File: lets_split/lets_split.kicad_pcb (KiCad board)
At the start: 2 copper layers, 114.2 x 82 mm, 79 parts, among them J1 Speaker, P1 USB-rewire, P2 USB_OTG, P3 WS2812, P4 TRRS jack, SW1 SW_PUSH, SW10 SW_PUSH, SW11 SW_PUSH, SW12 SW_PUSH, SW13 SW_PUSH, SW14 SW_PUSH, SW15 SW_PUSH, SW16 SW_PUSH, SW17 SW_PUSH, SW18 SW_PUSH, SW19 SW_PUSH, SW2 SW_PUSH, SW20 SW_PUSH, SW21 SW_PUSH, SW22 SW_PUSH, SW23 SW_PUSH, SW24 SW_PUSH, SW3 SW_PUSH, SW4 SW_PUSH, SW5 SW_PUSH, SW6 SW_PUSH, SW7 SW_PUSH, SW8 SW_PUSH, SW9 SW_PUSH, U1 ArduinoProMicro

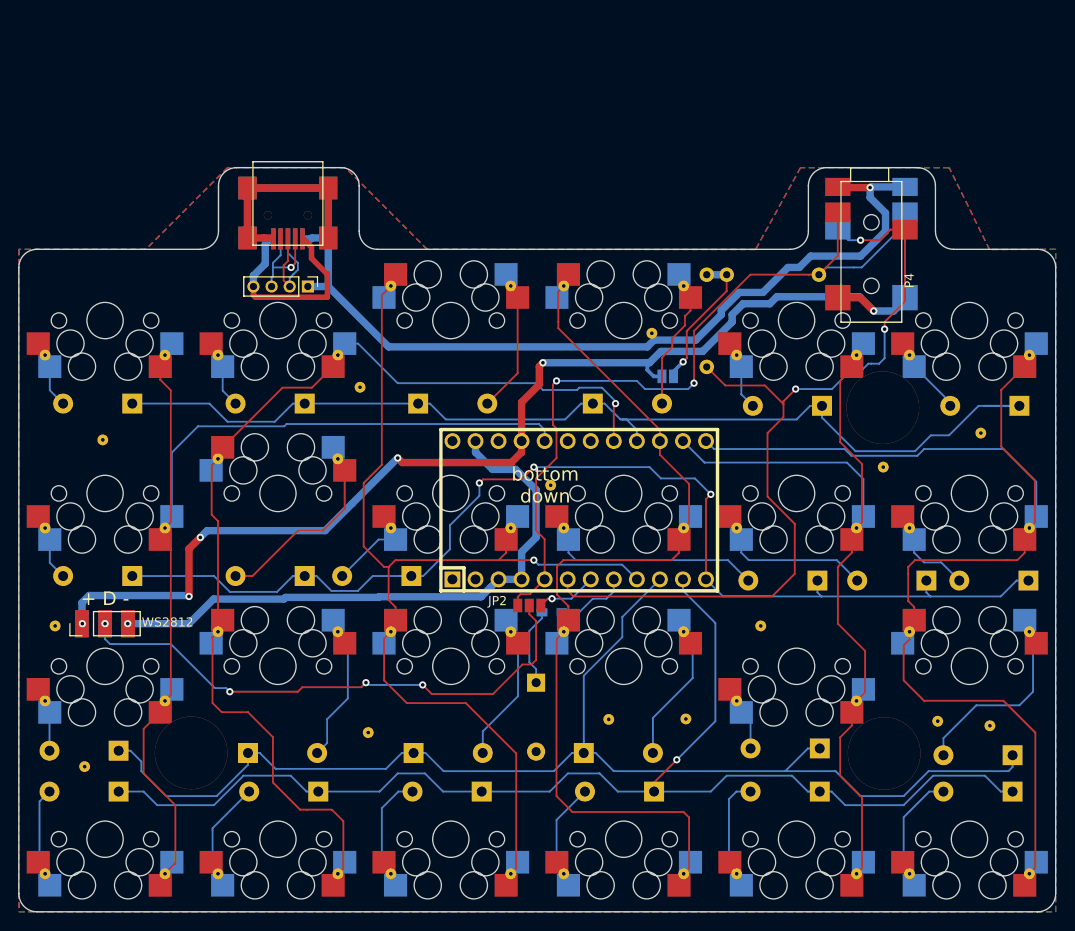
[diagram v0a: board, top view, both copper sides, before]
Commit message: Did a few small changes to routing
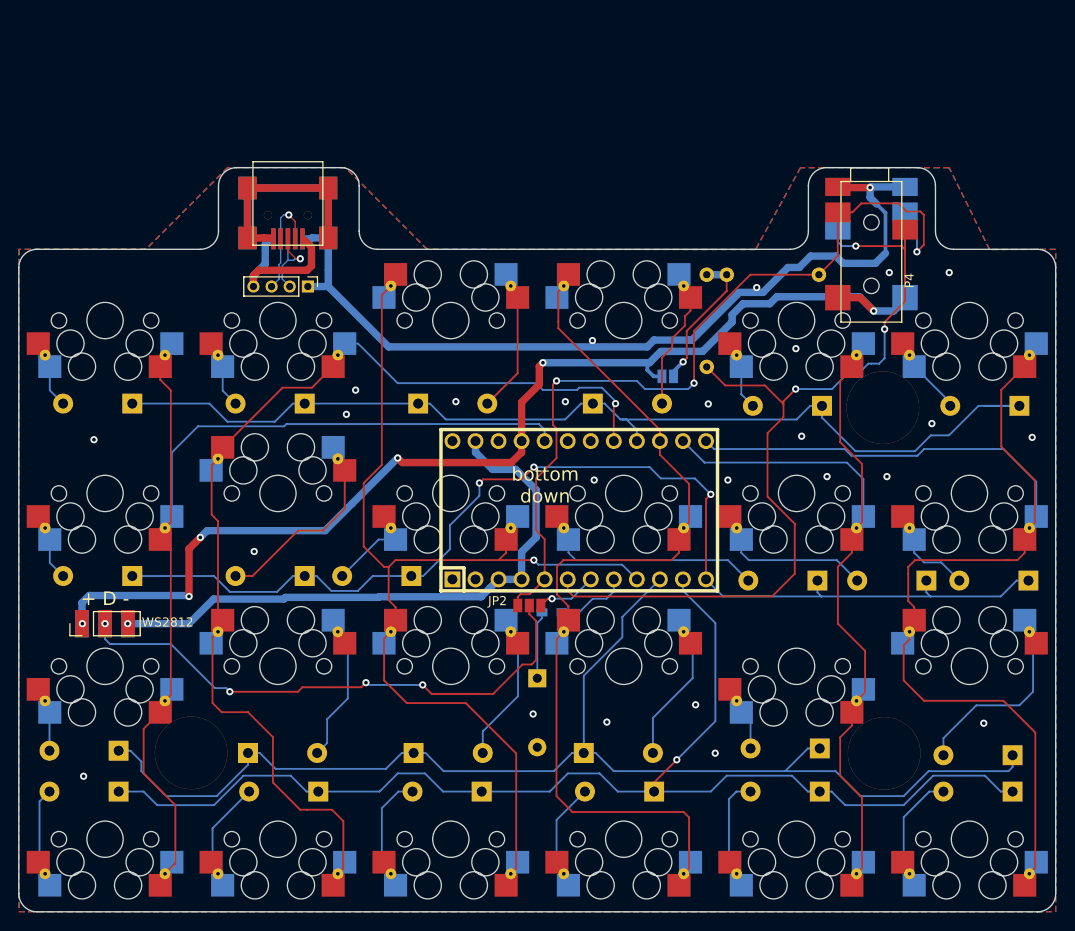
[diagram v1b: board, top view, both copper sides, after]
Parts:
- removed the REF** at (139.6, 91.0)
- removed the REF** at (176.2, 89.0)
- removed the REF** at (150.8, 74.2)
- removed the REF** at (88.2, 122.0)
- removed the REF** at (85.0, 106.5)
- removed the REF** at (90.2, 86.0)
- removed the REF** at (118.6, 80.2)
- removed the REF** at (188.0, 117.5)
- removed the REF** at (154.5, 116.8)
- removed the REF** at (182.2, 117.0)
- removed the REF** at (162.8, 106.5)
- removed the REF** at (119.5, 118.2)
- removed the REF** at (146.0, 116.8)
- removed the REF** at (187.0, 85.2)
- P3: value WS2812 -> WS2812-Strip
- moved J1 0.50 mm to (138.1, 112.3)
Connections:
- P2 pad 4: (no net) -> Net-(P2-Pad4)
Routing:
- net SDA: track 86.9 -> 93.5 mm, vias 2 -> 3
- net Net-(P1-Pad4): track 23.4 -> 18.1 mm
- net GND: track 201.0 -> 202.9 mm, vias 2 -> 27
- net /D+: track 11.8 -> 10.3 mm, vias 0 -> 1
- net Net-(J1-Pad1): track 8.64 -> 7.49 mm
- net /D-: track 11.0 -> 11.9 mm
- net SCL/D3: track 95.3 -> 96.0 mm
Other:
- net class Default: trace_width 0.25 -> 0.1524

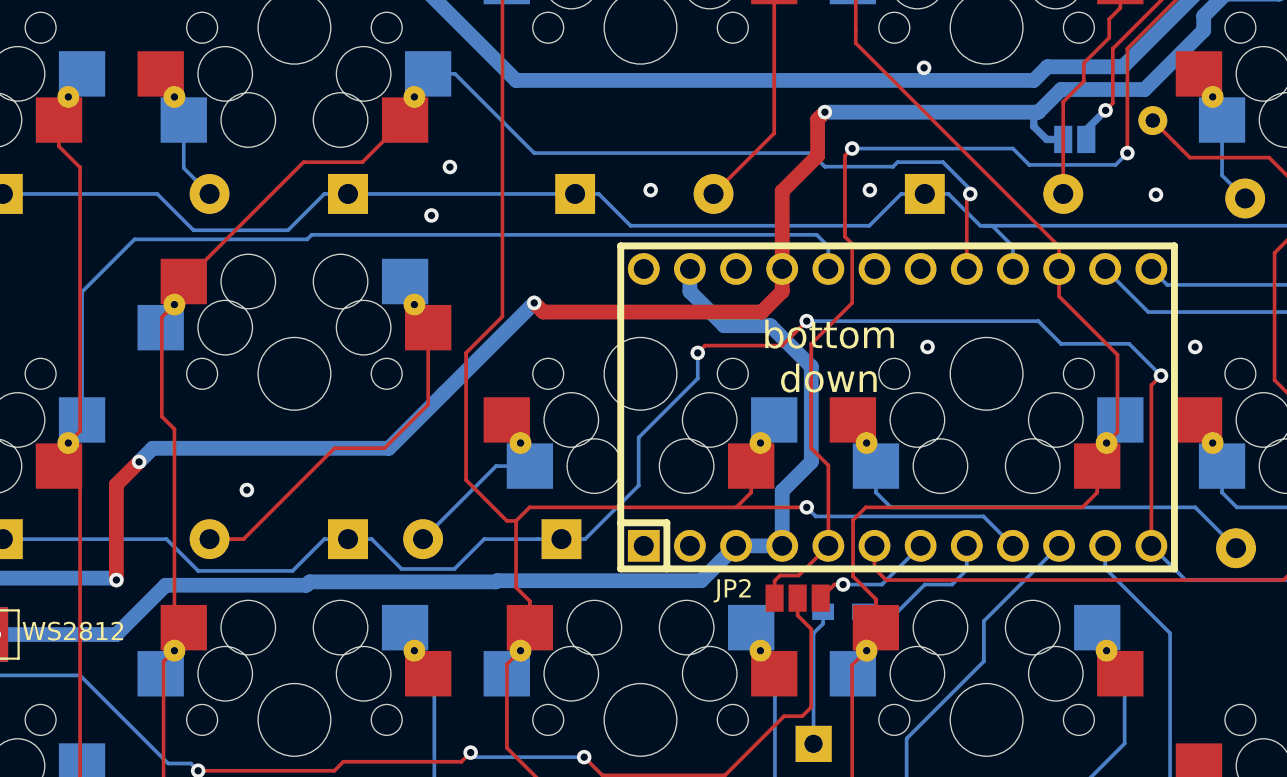
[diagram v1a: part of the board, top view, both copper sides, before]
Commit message: Fixed a broken gnd path
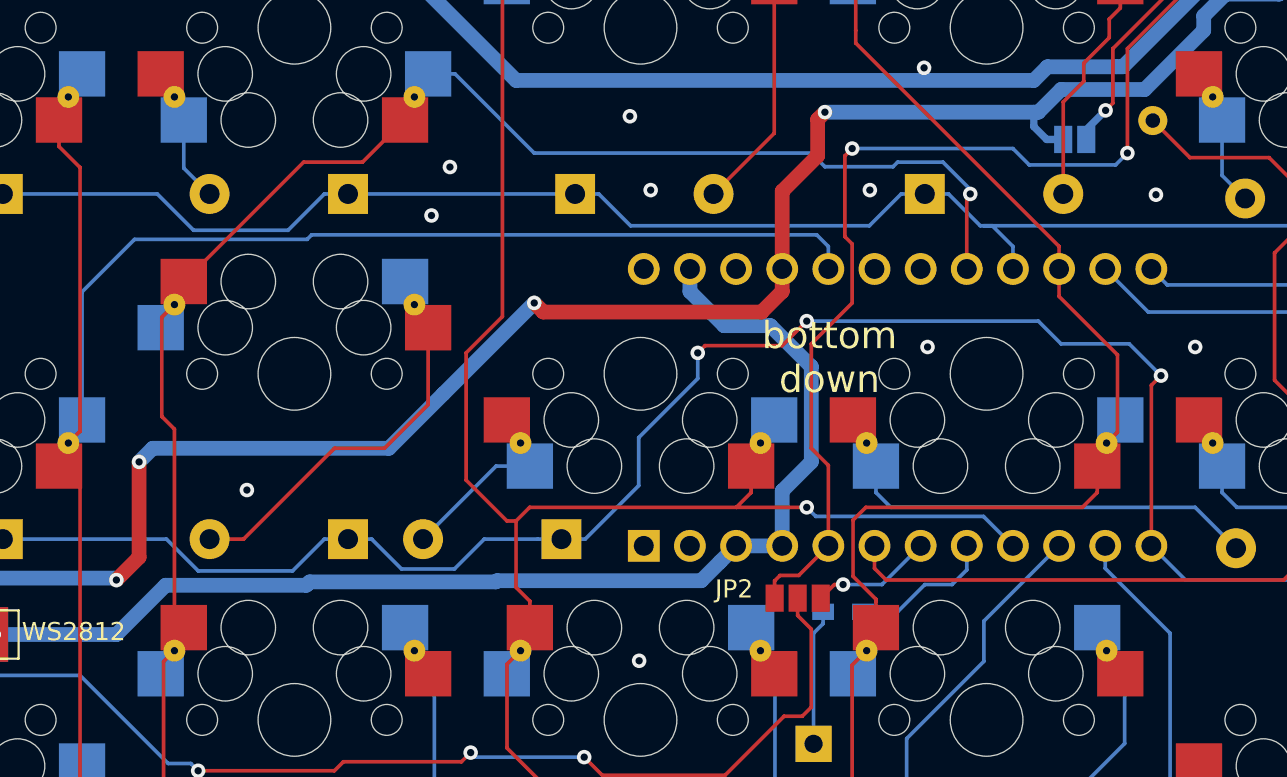
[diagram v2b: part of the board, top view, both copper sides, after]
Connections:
- P2 pad 4: Net-(P2-Pad4) -> (no net) (x2)
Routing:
- net GND: vias 27 -> 29
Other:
- net class Default: trace_width 0.1524 -> 0.25

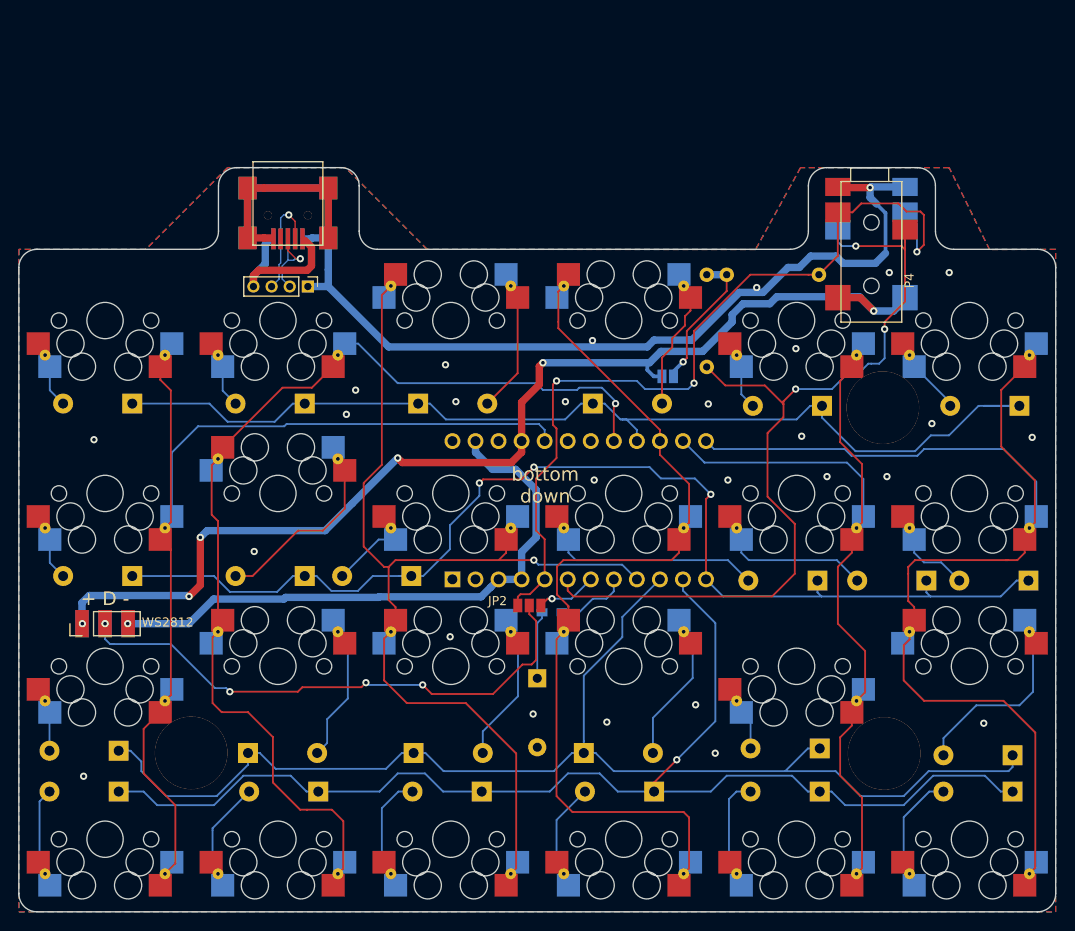
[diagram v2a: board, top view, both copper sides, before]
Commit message: Added speaker symbol
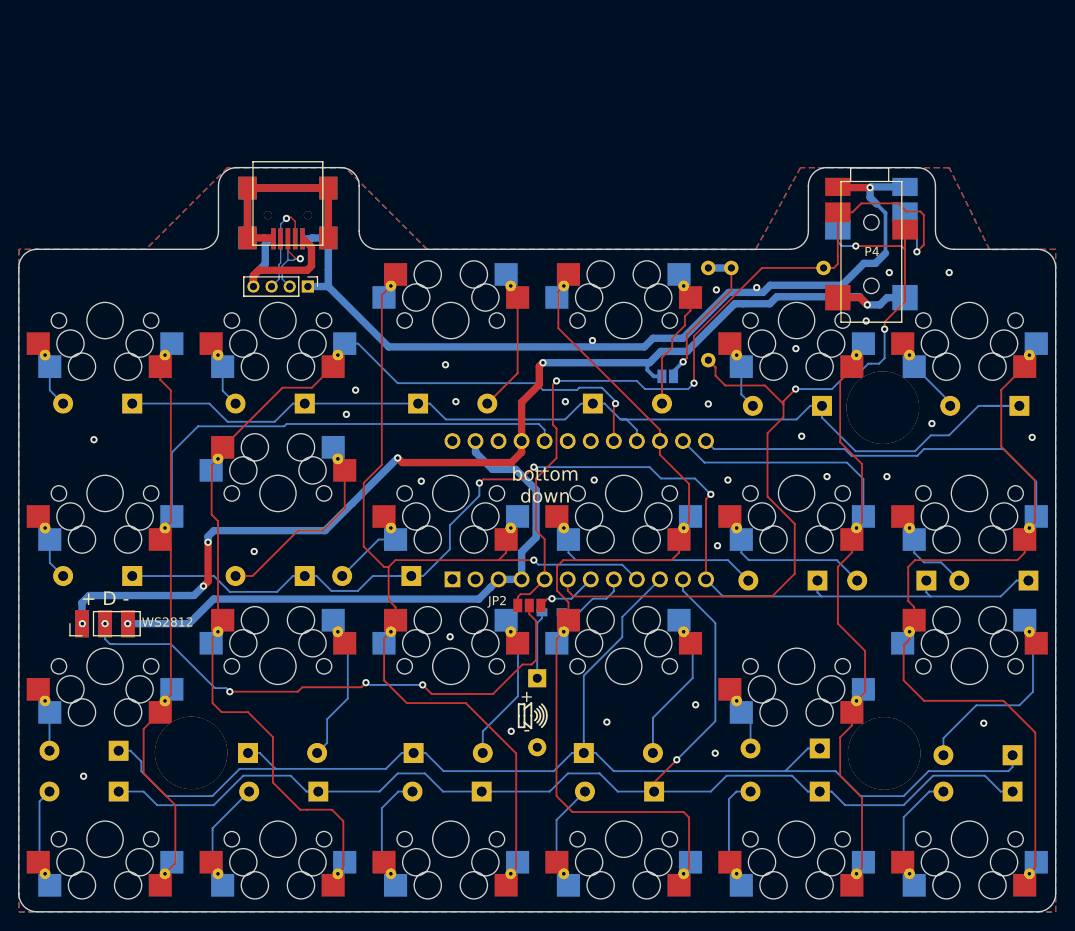
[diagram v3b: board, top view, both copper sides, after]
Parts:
- P3: value WS2812-Strip -> WS2812
- moved R1 0.90 mm to (159.5, 67.1)
- moved R2 0.76 mm to (157.0, 67.1)
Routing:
- net VCC: track 124.8 -> 122.4 mm
- net row2: track 139.1 -> 140.6 mm
- net Net-(JP1-Pad2): track 15.8 -> 17.1 mm
- net SCL/D3: track 96.0 -> 96.7 mm
- net GND: track 202.9 -> 202.2 mm, vias 29 -> 32
- net /D-: track 11.9 -> 11.3 mm
- net (no net): vias 0 -> 1
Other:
- rule trace_min: 0.008 -> 0.1524
- board text added: "+"
- board text added: "-"

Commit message: Changed footpring designations for possible PCBA in the future
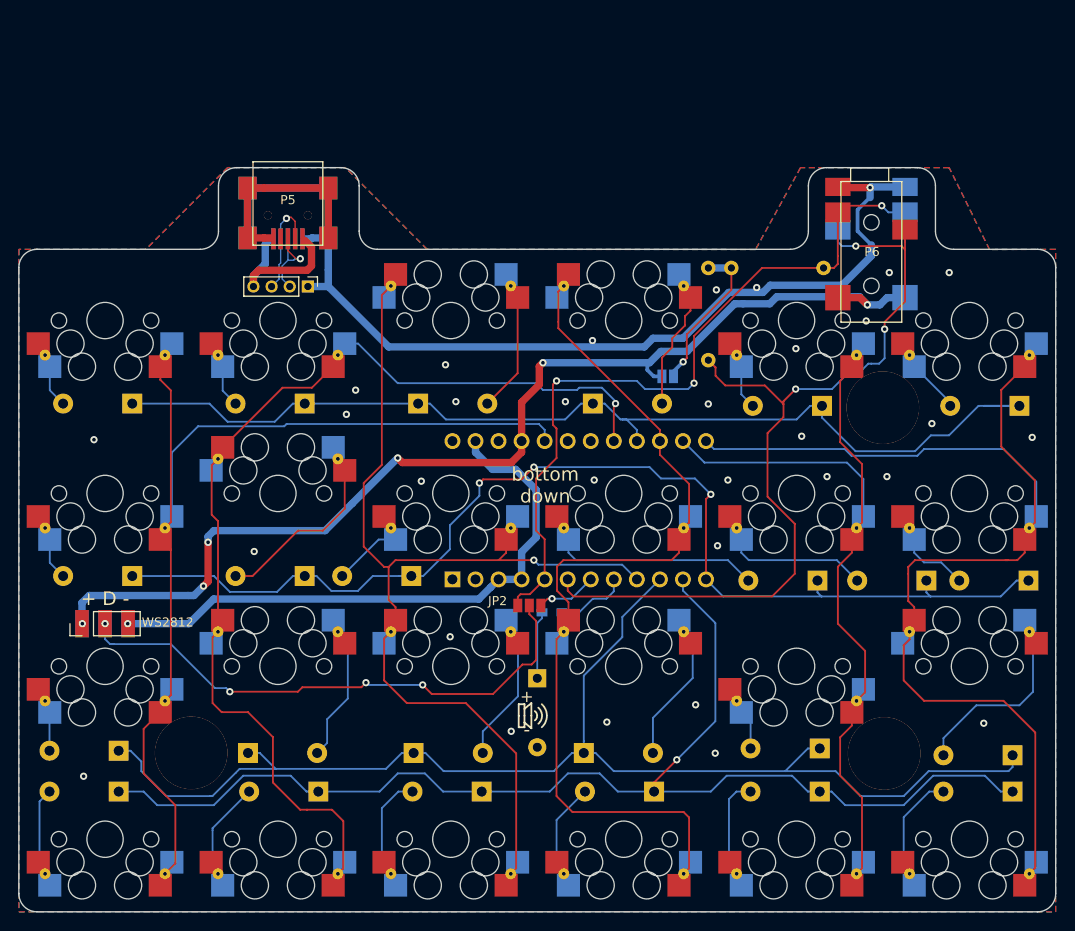
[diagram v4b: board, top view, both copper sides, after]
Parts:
- P3: value WS2812 -> WS2812-Strip
- P4: value TRRS jack -> Conn_01x04
- P6: renamed from P4; value TRRS jack -> Conn_01x04
- R3: value 150 -> 200
- renumbered P2 to P5
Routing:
- net SDA: track 93.7 -> 82.0 mm
- net GND: track 202.2 -> 201.3 mm

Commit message: Moved TRRS connector to clear switches
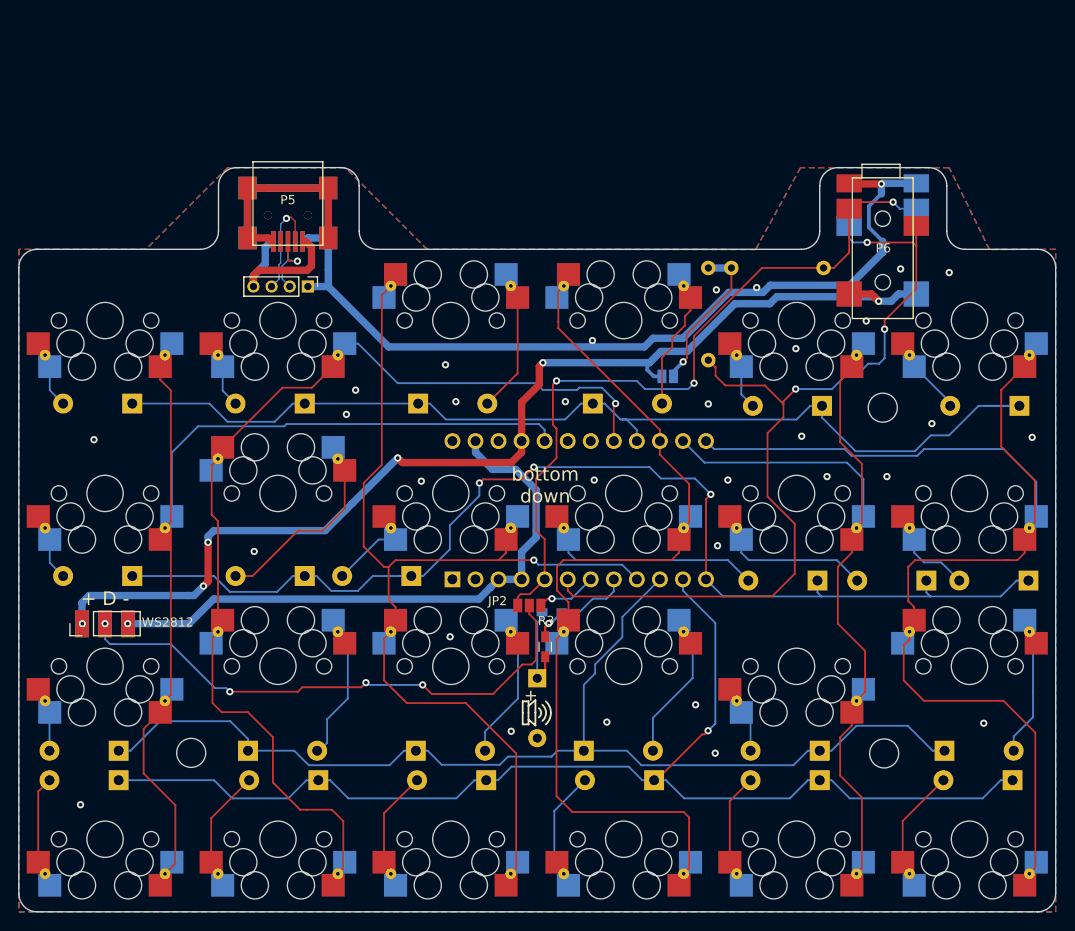
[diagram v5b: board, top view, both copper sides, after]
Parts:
- added R3: 200, Resistors_SMD:R_0603_HandSoldering, F.Cu at (139.0, 108.8)
- moved D23 7.52 mm to (183.0, 120.2), turned to 0 degrees
- moved D12 1.35 mm to (132.5, 123.5)
- moved P4 1.31 mm to (176.2, 64.9)
- moved P6 1.31 mm to (176.2, 64.9)
- moved D16 1.25 mm to (151.0, 123.5)
- moved D20 1.25 mm to (169.2, 123.5)
- moved D24 1.25 mm to (190.5, 123.5)
- moved D4 1.25 mm to (92.0, 123.5)
- moved D8 1.25 mm to (114.0, 123.5)
- moved D11 0.35 mm to (124.8, 120.2)
- moved D15 0.25 mm to (143.2, 120.2)
- moved D19 0.25 mm to (169.2, 120.2)
- moved D7 0.25 mm to (106.2, 120.2)
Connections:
- P2 pad 4: (no net) -> Net-(P2-Pad4)
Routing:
- net row2: track 140.6 -> 124.3 mm
- net Net-(D23-Pad2): track 23.7 -> 17.2 mm
- net Net-(R3-Pad1): track 7.99 -> 11.6 mm, vias 0 -> 1
- net row3: track 136.3 -> 133.3 mm
- net Net-(J1-Pad1): track 7.49 -> 10.2 mm
- net GND: track 201.3 -> 203.1 mm
- net Net-(D16-Pad2): track 13.8 -> 15.2 mm
- net Net-(D20-Pad2): track 14.4 -> 13.1 mm
- net Net-(D12-Pad2): track 14.8 -> 13.6 mm
- net Net-(D24-Pad2): track 15.1 -> 14.0 mm
- net VCC: track 122.4 -> 123.5 mm
- net SDA: track 82.0 -> 83.1 mm
- net SCL/D3: track 96.7 -> 97.6 mm
- net Net-(P1-Pad4): track 18.1 -> 17.4 mm
- net /D+: track 10.3 -> 9.75 mm
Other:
- outline, holes or cut-outs redrawn
- net class Default: trace_width 0.25 -> 0.1524
- board text removed: "-"
